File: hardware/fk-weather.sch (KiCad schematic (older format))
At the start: 97 parts, among them J1 MICRO-USB, J2 CONN_01X03, J3 CONN_01X06, J4 CONN_01X04, J5 Conn_01x01, J6 CONN-HDR-2x5, J7 Conn_01x01, J8 Conn_01x01, J9 Conn_01x01, M1 MOUNT_HOLE, M2 MOUNT_HOLE, M3 MOUNT_HOLE, M4 MOUNT_HOLE, Q1 2N7002LT1G, Q2 2N7002LT1G, Q3 2N7002LT1G, Q4 2N7002LT1G, SW1 SPNO, U1 ATSAMD21G18A-AU, U101 TSL2591, U102 MPL3115A2, U103 BNO055, U104 SHT31, U2 MCP1700T-XXX2E, U3 MAX4466, Y1 FC-135, Y101 FC-135

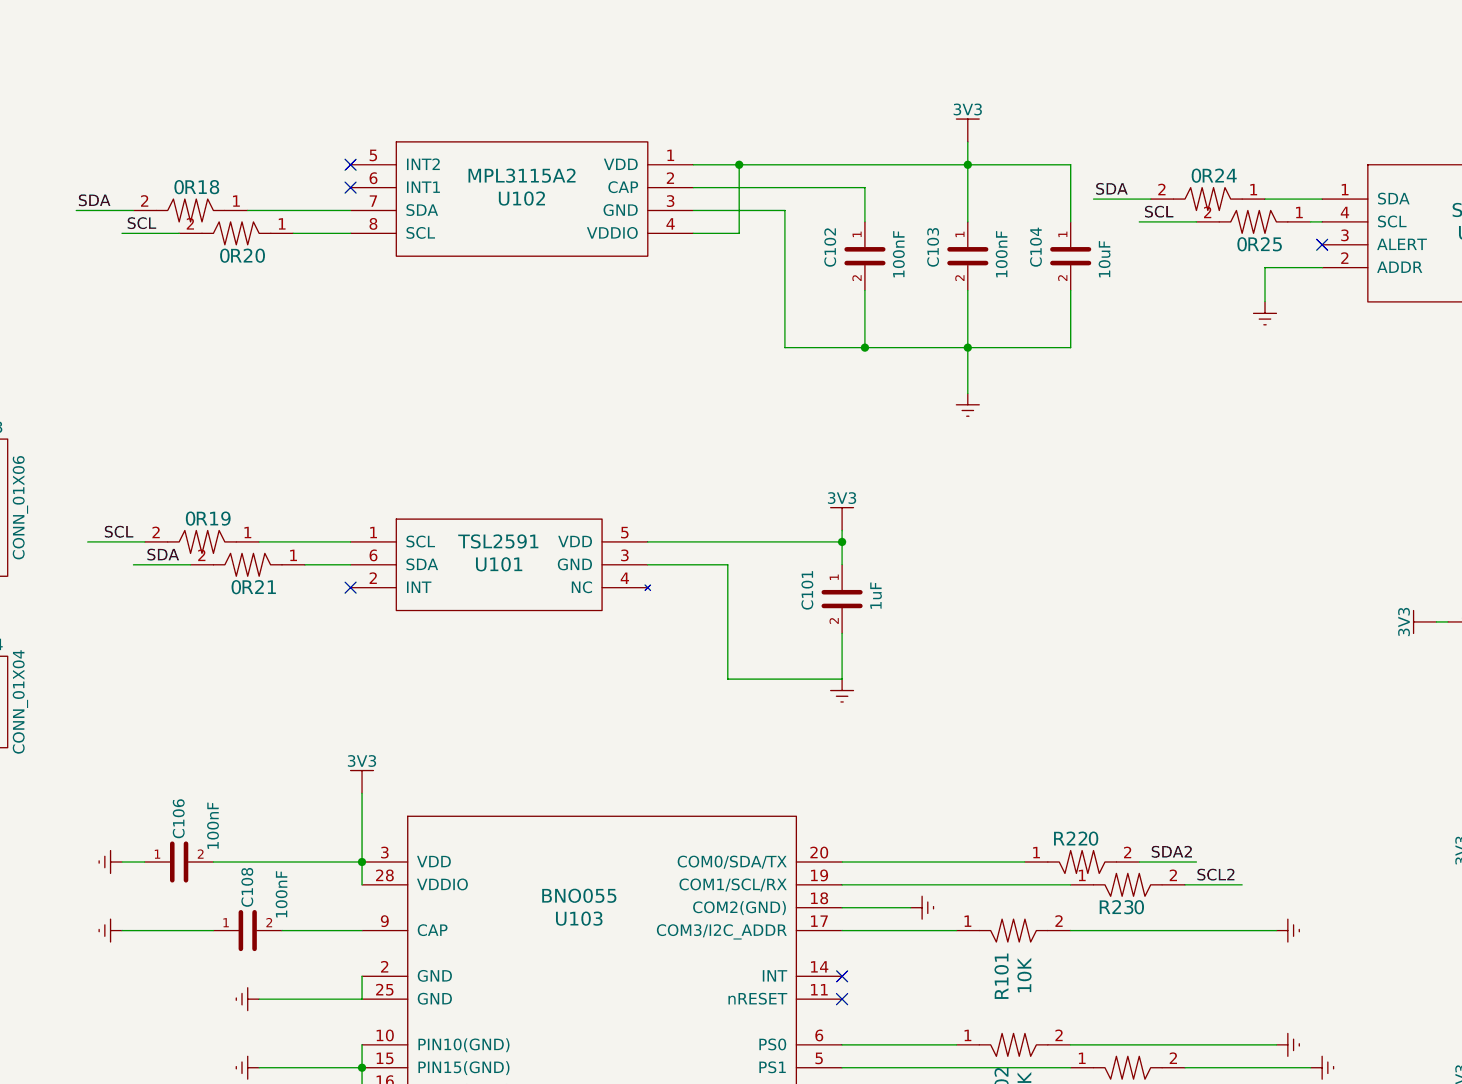
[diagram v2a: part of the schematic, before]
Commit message: Fixing up some parts to work with our BOM scripts.
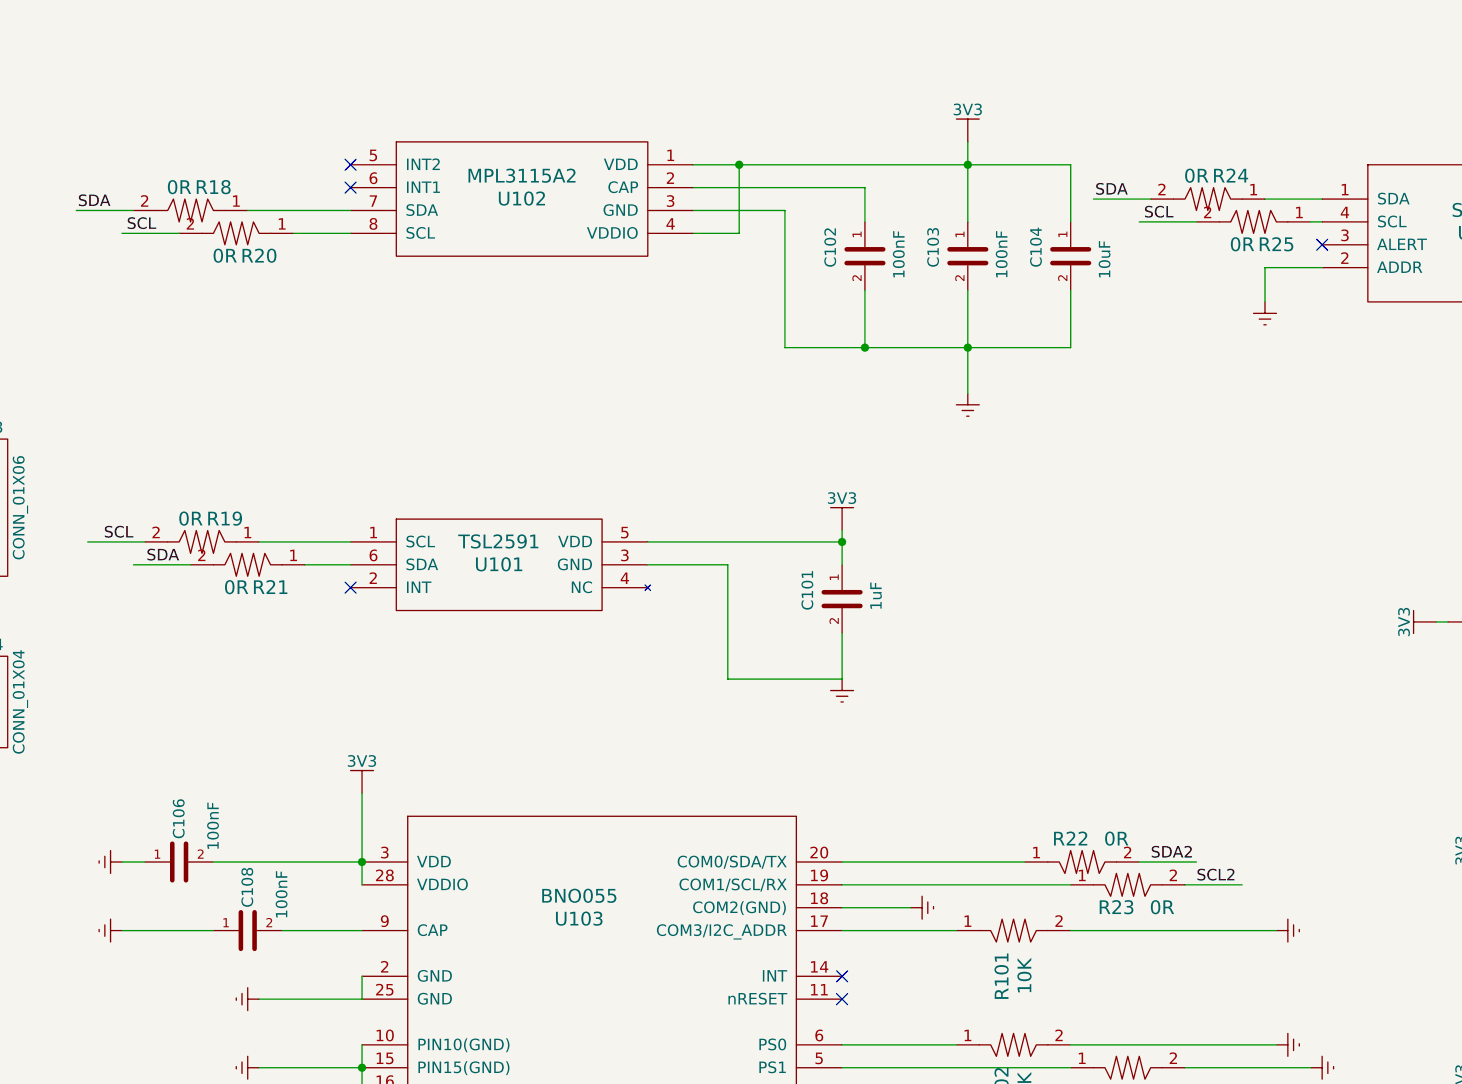
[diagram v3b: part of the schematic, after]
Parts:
- R18, R19, R20, R21, R22, R23, R24, R25: value 0 -> 0R; spn1 603-RC0603FR-0710KL -> (none)

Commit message: Adding flash memory to the schematic.
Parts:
- added C18: 100nF, Capacitors_SMD:C_0603_HandSoldering, symbol CAPACITOR-CERAMIC
- added U4: S25FL1xxK0XM, RocketScreamKicadLibrary:SOIC-8-N, symbol S25FL1xxK0XM
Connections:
- wire segments 289 -> 301
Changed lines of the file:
@@
 LIBS:conn
 LIBS:conservify
+LIBS:RocketScreamKicadLibrary
 LIBS:fk-weather-cache
 EELAYER 25 0
@@
 NoConn ~ 2200 5200
 NoConn ~ 1700 5200
+$Comp
+L S25FL1xxK0XM U4
+U 1 1 5A1C9BD4
+P 9700 9750
+F 0 "U4" H 9700 10050 60  0000 C CNN
+F 1 "S25FL1xxK0XM" H 9700 9450 60  0000 C CNN
+F 2 "RocketScreamKicadLibrary:SOIC-8-N" H 9700 9350 60  0001 C CNN
+F 3 "" H 9500 9800 60  0000 C CNN
+	1    9700 9750
+	1    0    0    -1
+$EndComp
+$Comp
+L 3V3 #PWR068
+U 1 1 5A1C9D8B
+P 8550 9450
+F 0 "#PWR068" H 8550 9300 50  0001 C CNN
+F 1 "3V3" H 8550 9590 50  0000 C CNN
+F 2 "" H 8550 9450 60  0000 C CNN
+F 3 "" H 8550 9450 60  0000 C CNN
+	1    8550 9450
+	1    0    0    -1
+$EndComp
+$Comp
+L 3V3 #PWR069
+U 1 1 5A1C9EBC
+P 10550 9450
+F 0 "#PWR069" H 10550 9300 50  0001 C CNN
+F 1 "3V3" H 10550 9590 50  0000 C CNN
+F 2 "" H 10550 9450 60  0000 C CNN
+F 3 "" H 10550 9450 60  0000 C CNN
+	1    10550 9450
+	1    0    0    -1
+$EndComp
+$Comp
+L CAPACITOR-CERAMIC C18
+U 1 1 5A1CAC3A
+P 10900 9600
+F 0 "C18" H 11000 9600 50  0000 L CNN
+F 1 "100nF" H 10950 9450 50  0000 L CNN
+F 2 "Capacitors_SMD:C_0603_HandSoldering" H 10900 9400 30  0001 C CNN
+F 3 "" H 10900 9600 60  0000 C CNN
+F 4 "0" H 11000 9700 50  0001 C CNN "price"
+F 5 "81-GRM39X104K50D" H 8800 2800 50  0001 C CNN "spn1"
+F 6 "mouser" H 8800 2800 50  0001 C CNN "supplier1"
+	1    10900 9600
+	0    -1   -1   0
+$EndComp
+Text Label 10450 9800 0    60   ~ 0
+SCK
+Text Label 10450 9900 0    60   ~ 0
+MOSI
+Text Label 8750 9700 0    60   ~ 0
+MISO
+Text Label 8750 9600 0    60   ~ 0
+D5
+Wire Wire Line
+	9150 9600 8750 9600
+Wire Wire Line
+	8750 9700 9150 9700
+Wire Wire Line
+	10250 9800 10750 9800
+Wire Wire Line
+	10750 9900 10250 9900
+Wire Wire Line
+	10750 9600 10250 9600
+Wire Wire Line
+	10550 9450 10550 9700
+Connection ~ 10550 9600
+Wire Wire Line
+	10550 9700 10250 9700
+Wire Wire Line
+	9150 9800 8550 9800
+Wire Wire Line
+	8550 9800 8550 9450
+$Comp
+L GND #PWR070
+U 1 1 5A1CCCEE
+P 9050 10200
+F 0 "#PWR070" H 9050 9950 50  0001 C CNN
+F 1 "GND" H 9050 10050 50  0001 C CNN
+F 2 "" H 9050 10200 60  0000 C CNN
+F 3 "" H 9050 10200 60  0000 C CNN
+	1    9050 10200
+	1    0    0    -1
+$EndComp
+Wire Wire Line
+	9150 9900 9050 9900
+Wire Wire Line
+	9050 9900 9050 10200
+$Comp
+L GND #PWR071
+U 1 1 5A1CDAB1
+P 11200 9600
+F 0 "#PWR071" H 11200 9350 50  0001 C CNN
+F 1 "GND" H 11200 9450 50  0001 C CNN
+F 2 "" H 11200 9600 60  0000 C CNN
+F 3 "" H 11200 9600 60  0000 C CNN
+	1    11200 9600
+	0    -1   -1   0
+$EndComp
+Wire Wire Line
+	11200 9600 11050 9600
 $EndSCHEMATC

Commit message: Adding flash memory to PCB. Plotting.
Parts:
- removed J4: CONN_01X04, Socket_Strips:Socket_Strip_Straight_1x04_Pitch2.54mm, symbol CONN_01X04
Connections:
- wire segments 301 -> 297
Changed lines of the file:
@@
 LIBS:conn
 LIBS:conservify
-LIBS:RocketScreamKicadLibrary
 LIBS:fk-weather-cache
 EELAYER 25 0
@@
 	1    6650 3150
 	1    0    0    -1
-$EndComp
-$Comp
-L CONN_01X04 J4
-U 1 1 59BCDA28
-P 7300 3750
-F 0 "J4" H 7300 4000 50  0000 C CNN
-F 1 "CONN_01X04" V 7400 3750 50  0000 C CNN
-F 2 "Socket_Strips:Socket_Strip_Straight_1x04_Pitch2.54mm" H 7300 3750 50  0001 C CNN
-F 3 "" H 7300 3750 50  0001 C CNN
-F 4 "0" H 7300 4100 50  0001 C CNN "price"
-	1    7300 3750
-	1    0    0    -1
-$EndComp
-$Comp
-L 3V3 #PWR061
-U 1 1 59BCEEAB
-P 6750 3600
-F 0 "#PWR061" H 6750 3450 50  0001 C CNN
-F 1 "3V3" H 6750 3740 50  0000 C CNN
-F 2 "" H 6750 3600 60  0000 C CNN
-F 3 "" H 6750 3600 60  0000 C CNN
-	1    6750 3600
-	1    0    0    -1
-$EndComp
-$Comp
-L GND #PWR062
-U 1 1 59BCF3C6
-P 6750 3700
-F 0 "#PWR062" H 6750 3450 50  0001 C CNN
-F 1 "GND" H 6750 3550 50  0001 C CNN
-F 2 "" H 6750 3700 60  0000 C CNN
-F 3 "" H 6750 3700 60  0000 C CNN
-	1    6750 3700
-	0    1    1    0
 $EndComp
 $Comp
@@
 Text Label 2350 3650 0    50   ~ 0
 D13
-Text Label 6800 3900 0    50   ~ 0
-D6
-Text Label 6800 3800 0    50   ~ 0
-D5
 Text Label 8100 3150 2    50   ~ 0
 SDA
@@
 	7100 3150 6650 3150
 Wire Wire Line
-	7100 3700 6750 3700
-Wire Wire Line
-	6750 3800 7100 3800
-Wire Wire Line
-	7100 3900 6750 3900
-Wire Wire Line
-	6750 3600 7100 3600
-Wire Wire Line
 	12850 1850 13100 1850

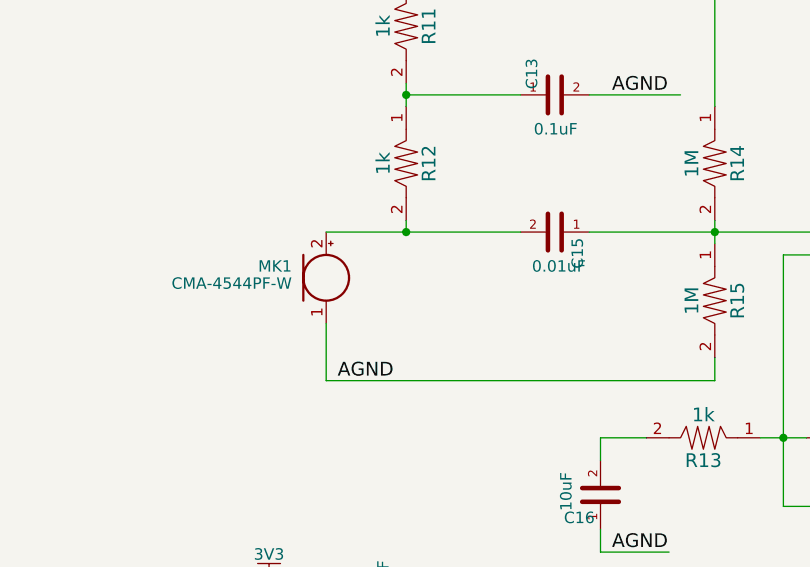
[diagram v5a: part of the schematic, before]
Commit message: Adding another breakout for the MIC to attach a header to for probing.
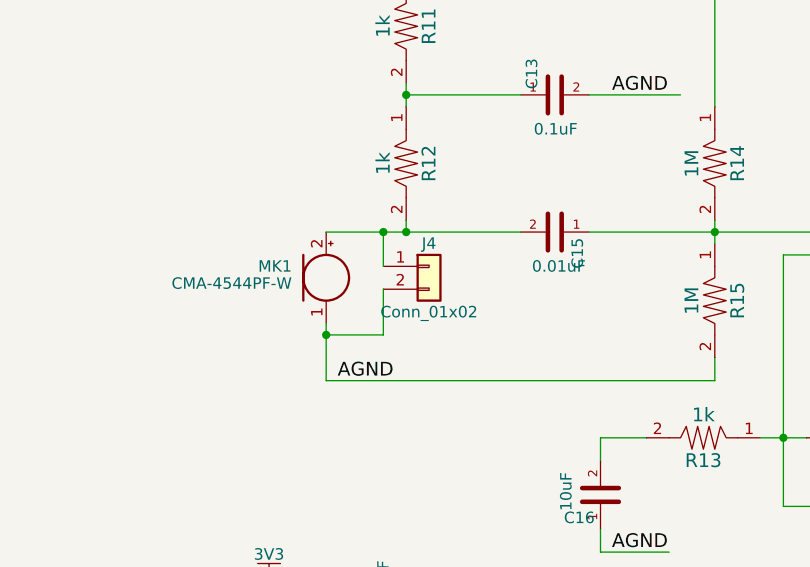
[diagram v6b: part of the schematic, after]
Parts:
- added J4: Conn_01x02, Socket_Strips:Socket_Strip_Straight_2x01_Pitch2.54mm, symbol Conn_01x02
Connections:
- wire segments 297 -> 300
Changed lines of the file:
@@
 LIBS:conn
 LIBS:conservify
+LIBS:RocketScreamKicadLibrary
 LIBS:fk-weather-cache
 EELAYER 25 0
@@
 $EndComp
 $Comp
-L GND #PWR063
+L GND #PWR061
 U 1 1 59CBF65F
 P 12850 2000
-F 0 "#PWR063" H 12850 1750 50  0001 C CNN
+F 0 "#PWR061" H 12850 1750 50  0001 C CNN
 F 1 "GND" H 12850 1850 50  0001 C CNN
 F 2 "" H 12850 2000 60  0000 C CNN
@@
 $EndComp
 $Comp
-L 3V3 #PWR064
+L 3V3 #PWR062
 U 1 1 59FC34E5
 P 6350 5450
-F 0 "#PWR064" H 6350 5300 50  0001 C CNN
+F 0 "#PWR062" H 6350 5300 50  0001 C CNN
 F 1 "3V3" H 6350 5590 50  0000 C CNN
 F 2 "" H 6350 5450 60  0000 C CNN
@@
 $EndComp
 $Comp
-L 3V3 #PWR065
+L 3V3 #PWR063
 U 1 1 59FC34EB
 P 6350 5800
-F 0 "#PWR065" H 6350 5650 50  0001 C CNN
+F 0 "#PWR063" H 6350 5650 50  0001 C CNN
 F 1 "3V3" H 6350 5940 50  0000 C CNN
 F 2 "" H 6350 5800 60  0000 C CNN
@@
 $EndComp
 $Comp
-L 3V3 #PWR066
+L 3V3 #PWR064
 U 1 1 59FC950C
 P 6350 6150
-F 0 "#PWR066" H 6350 6000 50  0001 C CNN
+F 0 "#PWR064" H 6350 6000 50  0001 C CNN
 F 1 "3V3" H 6350 6290 50  0000 C CNN
 F 2 "" H 6350 6150 60  0000 C CNN
@@
 $EndComp
 $Comp
-L 3V3 #PWR067
+L 3V3 #PWR065
 U 1 1 59FC9512
 P 6350 6500
-F 0 "#PWR067" H 6350 6350 50  0001 C CNN
+F 0 "#PWR065" H 6350 6350 50  0001 C CNN
 F 1 "3V3" H 6350 6640 50  0000 C CNN
 F 2 "" H 6350 6500 60  0000 C CNN
@@
 $EndComp
 $Comp
-L 3V3 #PWR068
+L 3V3 #PWR066
 U 1 1 5A1C9D8B
 P 8550 9450
-F 0 "#PWR068" H 8550 9300 50  0001 C CNN
+F 0 "#PWR066" H 8550 9300 50  0001 C CNN
 F 1 "3V3" H 8550 9590 50  0000 C CNN
 F 2 "" H 8550 9450 60  0000 C CNN
@@
 $EndComp
 $Comp
-L 3V3 #PWR069
+L 3V3 #PWR067
 U 1 1 5A1C9EBC
 P 10550 9450
-F 0 "#PWR069" H 10550 9300 50  0001 C CNN
+F 0 "#PWR067" H 10550 9300 50  0001 C CNN
 F 1 "3V3" H 10550 9590 50  0000 C CNN
 F 2 "" H 10550 9450 60  0000 C CNN
@@
 	8550 9800 8550 9450
 $Comp
-L GND #PWR070
+L GND #PWR068
 U 1 1 5A1CCCEE
 P 9050 10200
-F 0 "#PWR070" H 9050 9950 50  0001 C CNN
+F 0 "#PWR068" H 9050 9950 50  0001 C CNN
 F 1 "GND" H 9050 10050 50  0001 C CNN
 F 2 "" H 9050 10200 60  0000 C CNN
@@
 	9050 9900 9050 10200
 $Comp
-L GND #PWR071
+L GND #PWR069
 U 1 1 5A1CDAB1
 P 11200 9600
-F 0 "#PWR071" H 11200 9350 50  0001 C CNN
+F 0 "#PWR069" H 11200 9350 50  0001 C CNN
 F 1 "GND" H 11200 9450 50  0001 C CNN
 F 2 "" H 11200 9600 60  0000 C CNN
@@
 Wire Wire Line
 	11200 9600 11050 9600
+$Comp
+L Conn_01x02 J4
+U 1 1 5A3AF028
+P 11250 8050
+F 0 "J4" H 11250 8150 50  0000 C CNN
+F 1 "Conn_01x02" H 11250 7850 50  0000 C CNN
+F 2 "Socket_Strips:Socket_Strip_Straight_2x01_Pitch2.54mm" H 11250 8050 50  0001 C CNN
+F 3 "" H 11250 8050 50  0001 C CNN
+	1    11250 8050
+	1    0    0    -1
+$EndComp
+Wire Wire Line
+	11050 8050 11050 7900
+Connection ~ 11050 7900
+Wire Wire Line
+	11050 8150 11050 8350
+Wire Wire Line
+	11050 8350 10800 8350
+Connection ~ 10800 8350
 $EndSCHEMATC
